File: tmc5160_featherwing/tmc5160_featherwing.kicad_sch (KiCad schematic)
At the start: 0 parts

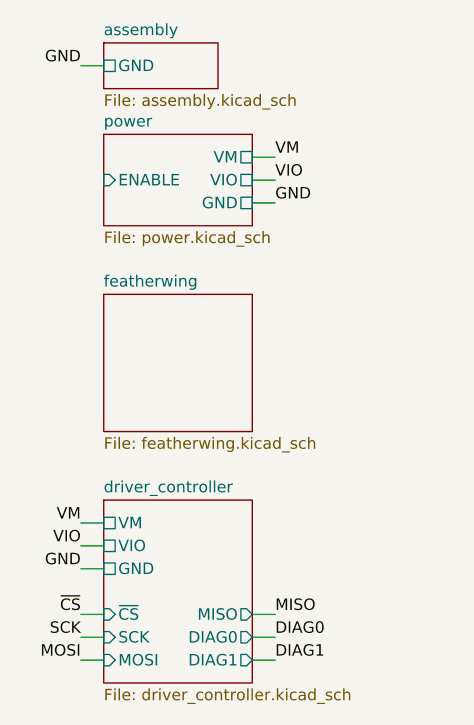
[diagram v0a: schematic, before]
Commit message: Add enable_fan
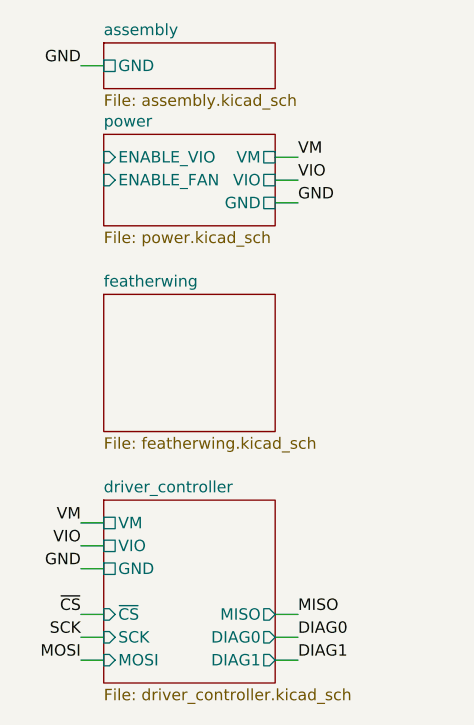
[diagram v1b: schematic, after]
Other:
- sheet power ports: added ENABLE_FAN, ENABLE_VIO; removed ENABLE
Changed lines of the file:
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@@
   (title_block
     (title "tmc5160_featherwing")
-    (date "2024-04-15")
+    (date "2024-04-16")
     (rev "1.0")
     (company "Howard Hughes Medical Institute")
@@
     (stroke (width 0) (type default))
   )
-  (wire (pts (xy 77.47 48.26) (xy 74.93 48.26))
+  (wire (pts (xy 80.01 48.26) (xy 77.47 48.26))
     (stroke (width 0) (type default))
   )
@@
     (stroke (width 0) (type default))
   )
-  (wire (pts (xy 74.93 104.14) (xy 77.47 104.14))
+  (wire (pts (xy 77.47 104.14) (xy 80.01 104.14))
     (stroke (width 0) (type default))
   )
@@
     (stroke (width 0) (type default))
   )
-  (wire (pts (xy 74.93 101.6) (xy 77.47 101.6))
+  (wire (pts (xy 77.47 101.6) (xy 80.01 101.6))
     (stroke (width 0) (type default))
   )
-  (wire (pts (xy 74.93 99.06) (xy 77.47 99.06))
+  (wire (pts (xy 77.47 99.06) (xy 80.01 99.06))
     (stroke (width 0) (type default))
   )
@@
     (stroke (width 0) (type default))
   )
-  (wire (pts (xy 77.47 53.34) (xy 74.93 53.34))
+  (wire (pts (xy 80.01 53.34) (xy 77.47 53.34))
     (stroke (width 0) (type default))
   )
-  (wire (pts (xy 77.47 50.8) (xy 74.93 50.8))
+  (wire (pts (xy 80.01 50.8) (xy 77.47 50.8))
     (stroke (width 0) (type default))
   )
-  (label "GND" (at 77.47 53.34 0) (fields_autoplaced)
+  (label "GND" (at 80.01 53.34 0) (fields_autoplaced)
     (effects (font (size 1.27 1.27)) (justify left bottom))
   )
-  (label "DIAG1" (at 77.47 104.14 0) (fields_autoplaced)
+  (label "DIAG1" (at 80.01 104.14 0) (fields_autoplaced)
     (effects (font (size 1.27 1.27)) (justify left bottom))
   )
-  (label "VIO" (at 77.47 50.8 0) (fields_autoplaced)
+  (label "VIO" (at 80.01 50.8 0) (fields_autoplaced)
     (effects (font (size 1.27 1.27)) (justify left bottom))
   )
@@
     (effects (font (size 1.27 1.27)) (justify right bottom))
   )
-  (label "DIAG0" (at 77.47 101.6 0) (fields_autoplaced)
+  (label "DIAG0" (at 80.01 101.6 0) (fields_autoplaced)
     (effects (font (size 1.27 1.27)) (justify left bottom))
   )
@@
     (effects (font (size 1.27 1.27)) (justify right bottom))
   )
-  (label "MISO" (at 77.47 99.06 0) (fields_autoplaced)
+  (label "MISO" (at 80.01 99.06 0) (fields_autoplaced)
     (effects (font (size 1.27 1.27)) (justify left bottom))
   )
@@
     (effects (font (size 1.27 1.27)) (justify right bottom))
   )
-  (label "VM" (at 77.47 48.26 0) (fields_autoplaced)
+  (label "VM" (at 80.01 48.26 0) (fields_autoplaced)
     (effects (font (size 1.27 1.27)) (justify left bottom))
   )
-  (sheet (at 58.42 86.36) (size 16.51 20.32) (fields_autoplaced)
+  (sheet (at 58.42 86.36) (size 19.05 20.32) (fields_autoplaced)
     (stroke (width 0.1524) (type solid))
     (fill (color 0 0 0 0.0000))
@@
       (effects (font (size 1.27 1.27)) (justify left))
     )
-    (pin "DIAG0" output (at 74.93 101.6 0)
+    (pin "DIAG0" output (at 77.47 101.6 0)
       (effects (font (size 1.27 1.27)) (justify right))
     )
-    (pin "DIAG1" output (at 74.93 104.14 0)
+    (pin "DIAG1" output (at 77.47 104.14 0)
       (effects (font (size 1.27 1.27)) (justify right))
     )
-    (pin "MISO" output (at 74.93 99.06 0)
+    (pin "MISO" output (at 77.47 99.06 0)
       (effects (font (size 1.27 1.27)) (justify right))
     )
@@
     )
   )
-  (sheet (at 58.42 35.56) (size 12.7 5.08) (fields_autoplaced)
+  (sheet (at 58.42 35.56) (size 19.05 5.08) (fields_autoplaced)
     (stroke (width 0.1524) (type solid))
     (fill (color 0 0 0 0.0000))
@@
     )
   )
-  (sheet (at 58.42 63.5) (size 16.51 15.24) (fields_autoplaced)
+  (sheet (at 58.42 63.5) (size 19.05 15.24) (fields_autoplaced)
     (stroke (width 0.1524) (type solid))
     (fill (color 0 0 0 0.0000))
@@
     )
   )
-  (sheet (at 58.42 45.72) (size 16.51 10.16) (fields_autoplaced)
+  (sheet (at 58.42 45.72) (size 19.05 10.16) (fields_autoplaced)
     (stroke (width 0.1524) (type solid))
     (fill (color 0 0 0 0.0000))
@@
       (effects (font (size 1.27 1.27)) (justify left top))
     )
-    (pin "GND" passive (at 74.93 53.34 0)
+    (pin "GND" passive (at 77.47 53.34 0)
       (effects (font (size 1.27 1.27)) (justify right))
     )
-    (pin "VM" passive (at 74.93 48.26 0)
+    (pin "VM" passive (at 77.47 48.26 0)
       (effects (font (size 1.27 1.27)) (justify right))
     )
-    (pin "VIO" passive (at 74.93 50.8 0)
+    (pin "VIO" passive (at 77.47 50.8 0)
       (effects (font (size 1.27 1.27)) (justify right))
     )
-    (pin "ENABLE" input (at 58.42 50.8 180)
+    (pin "ENABLE_VIO" input (at 58.42 48.26 180)
       (effects (font (size 1.27 1.27)) (justify left))
     )
+    (pin "ENABLE_FAN" input (at 58.42 50.8 180)
+      (effects (font (size 1.27 1.27)) (justify left))
+    )

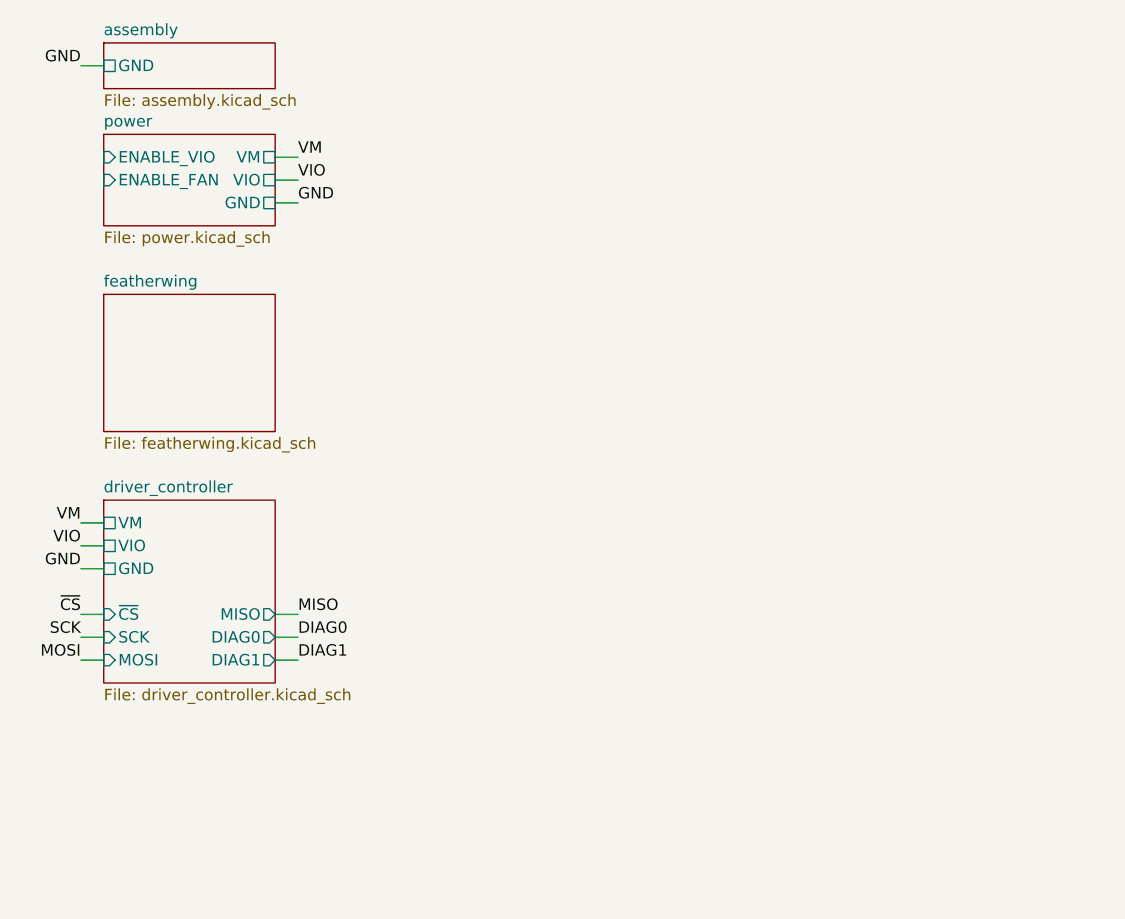
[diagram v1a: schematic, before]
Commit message: Add wires and labels
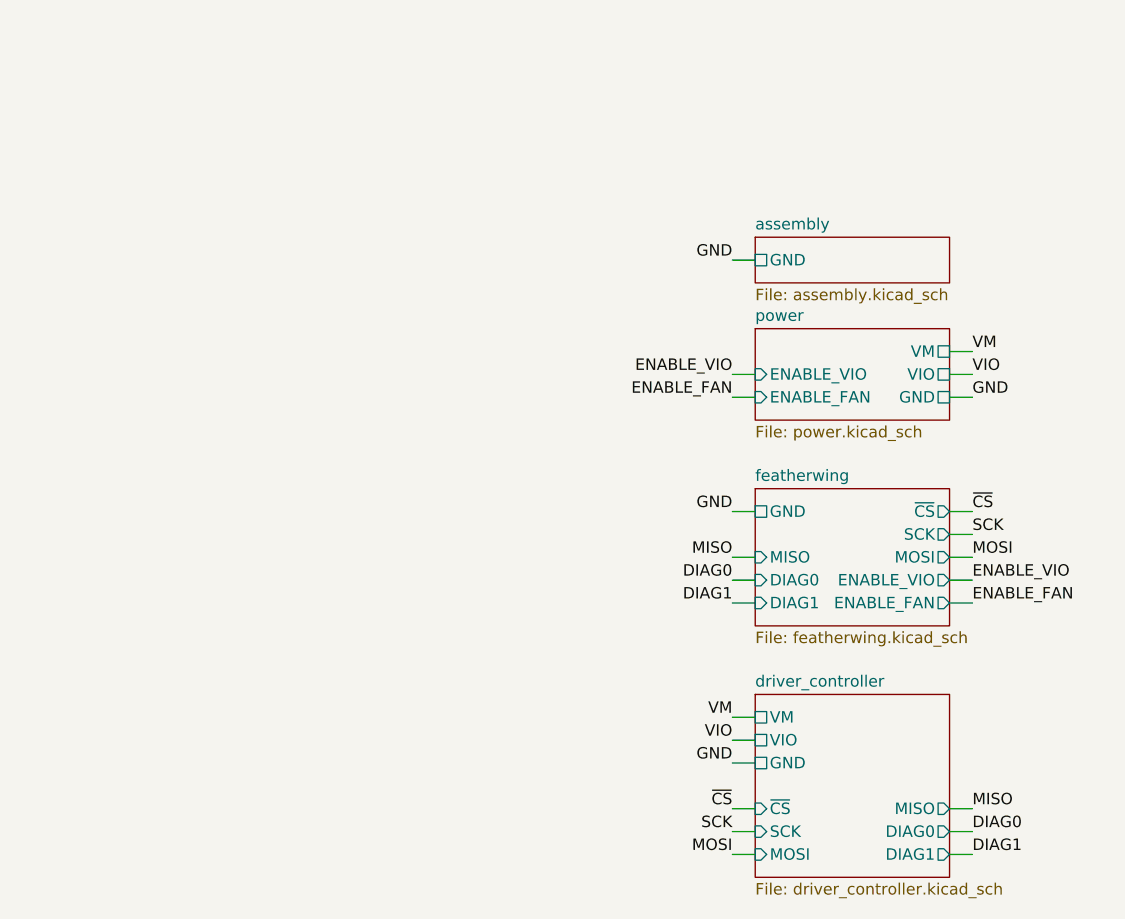
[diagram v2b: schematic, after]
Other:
- sheet featherwing ports: added DIAG0, DIAG1, ENABLE_FAN, ENABLE_VIO, GND, MISO, MOSI, SCK, ~{CS}; removed none
